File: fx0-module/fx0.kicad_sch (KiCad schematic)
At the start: 15 parts

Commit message: Add pcb draft
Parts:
- added U3: (no value), symbol promicro:ProMicro
- R1: value (none) -> 1K
- R2: value (none) -> 2K
- R3: value (none) -> 5K
- R4: value (none) -> 150K
- R5: value (none) -> 10K
- RF1: renamed from RF; value (none) -> idk
- RI1: renamed from RI; value (none) -> idk
- U2: value (none) -> Pico; footprint (none) -> RPi_Pico:RPi_Pico_SMD_TH
- ULIN1: renamed from ULIN; value (none) -> OPAMP
- renumbered UCVOUT to UCVOUT1
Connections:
- net CVOUT: now also U3.13 (B6)
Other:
- moved on the sheet: R3, R4, R5, UCVOUT1

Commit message: Finish up the fx0 board project
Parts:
- removed RF1, RI1: idk, symbol Device:R
- added C1: 1uF, Capacitor_SMD:C_0805_2012Metric_Pad1.18x1.45mm_HandSolder, symbol Device:C_Small
- added CLINOUT1: 33nF, Capacitor_SMD:C_0805_2012Metric_Pad1.18x1.45mm_HandSolder, symbol Device:C_Small
- added CLINOUT2: 10uF, Capacitor_SMD:C_0805_2012Metric_Pad1.18x1.45mm_HandSolder, symbol Device:C_Small
- added RLIN1, RLIN2, RLIN3: 100, Resistor_SMD:R_0805_2012Metric_Pad1.20x1.40mm_HandSolder, symbol Device:R
- added RLINOUT1, RRLINOUT5: 3.9k, Resistor_SMD:R_0805_2012Metric_Pad1.20x1.40mm_HandSolder, symbol Device:R
- added RLINOUT2: 10K, Resistor_SMD:R_0805_2012Metric_Pad1.20x1.40mm_HandSolder, symbol Device:R
- added RLINOUT3: 5K, Resistor_SMD:R_0805_2012Metric_Pad1.20x1.40mm_HandSolder, symbol Device:R
- added RLINOUT4: 150K, Resistor_SMD:R_0805_2012Metric_Pad1.20x1.40mm_HandSolder, symbol Device:R
- added ULINOUT1: LM358AD, Package_SO:SOP-8_3.9x4.9mm_P1.27mm, symbol pspice:OPAMP
- J1: value (none) -> Line IN; footprint (none) -> Connector_Wire:SolderWirePad_2x01_SMD_1x2mm
- J2: value (none) -> CV IN; footprint (none) -> Connector_Wire:SolderWirePad_2x01_SMD_1x2mm
- J3: value (none) -> Line OUT; footprint (none) -> Connector_Wire:SolderWirePad_2x01_SMD_1x2mm
- J4: value (none) -> CV OUT; footprint (none) -> Connector_Wire:SolderWirePad_2x01_SMD_1x2mm
- RCVIN1: renamed from R2; footprint (none) -> Resistor_SMD:R_0805_2012Metric_Pad1.20x1.40mm_HandSolder
- RCVIN2: renamed from R1; footprint (none) -> Resistor_SMD:R_0805_2012Metric_Pad1.20x1.40mm_HandSolder
- RCVOUT1: renamed from R5; footprint (none) -> Resistor_SMD:R_0805_2012Metric_Pad1.20x1.40mm_HandSolder
- RCVOUT2: renamed from R3; footprint (none) -> Resistor_SMD:R_0805_2012Metric_Pad1.20x1.40mm_HandSolder
- RRCVOUT3: renamed from R4; footprint (none) -> Resistor_SMD:R_0805_2012Metric_Pad1.20x1.40mm_HandSolder
- U1: value (none) -> SeeeduinoXIAO; footprint (none) -> Seeeduino XIAO KICAD:Seeeduino XIAO-MOUDLE14P-2.54-21X17.8MM
- U2: footprint RPi_Pico:RPi_Pico_SMD_TH -> MCU_RaspberryPi_and_Boards:RPi_Pico_SMD_TH
- U3: value (none) -> ProMicro; footprint (none) -> promicro:ProMicro
- UCVOUT1, ULIN1: value OPAMP -> LM358AD; footprint (none) -> Package_SO:SOP-8_3.9x4.9mm_P1.27mm
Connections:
- net 3V3: now also ULIN1.4 (V+), RLIN3.2
- net GND: now also J1.S, J2.S, J3.S, RCVIN1.1, U1.13 (GND), U2.18 (GND), U3.23 (GND), UCVOUT1.5 (V-), ULIN1.5 (V-), CLINOUT1.2, RLIN2.1, RLINOUT2.2, RRLINOUT5.1, ULINOUT1.5 (V-)
- net LINC: now also ULIN1.2 (-)
- net LOUT: now also RLINOUT1.2
- net 5V: now reaches U1.14 (5V)
- net 5V: now also U2.20 (GPIO15), U3.24 (RAW), UCVOUT1.4 (V+), ULINOUT1.4 (V+)
- net at ULIN1.1 (+): now also RLIN1.2, RLIN2.2, RLIN3.1; no longer J1.S
- net at J1.T: now also C1.1
- net LINOUTC: now reaches J3.T
- net LINOUTC: now also CLINOUT2.2, RRLINOUT5.2
- new net: CLINOUT2.1, RLINOUT4.2, ULINOUT1.3
- new net: CLINOUT1.1, RLINOUT1.1, ULINOUT1.1 (+)
- new net: RLINOUT2.1, RLINOUT3.1, ULINOUT1.2 (-)
- new net: C1.2, RLIN1.1
- new net: RLINOUT3.2, RLINOUT4.1
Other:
- note removed: "LINC = RF/RI*LINEIN"
- moved on the sheet: J1, J2, J3, J4, RCVIN1, RCVIN2, RCVOUT1, RCVOUT2, RRCVOUT3, U1, U2, U3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

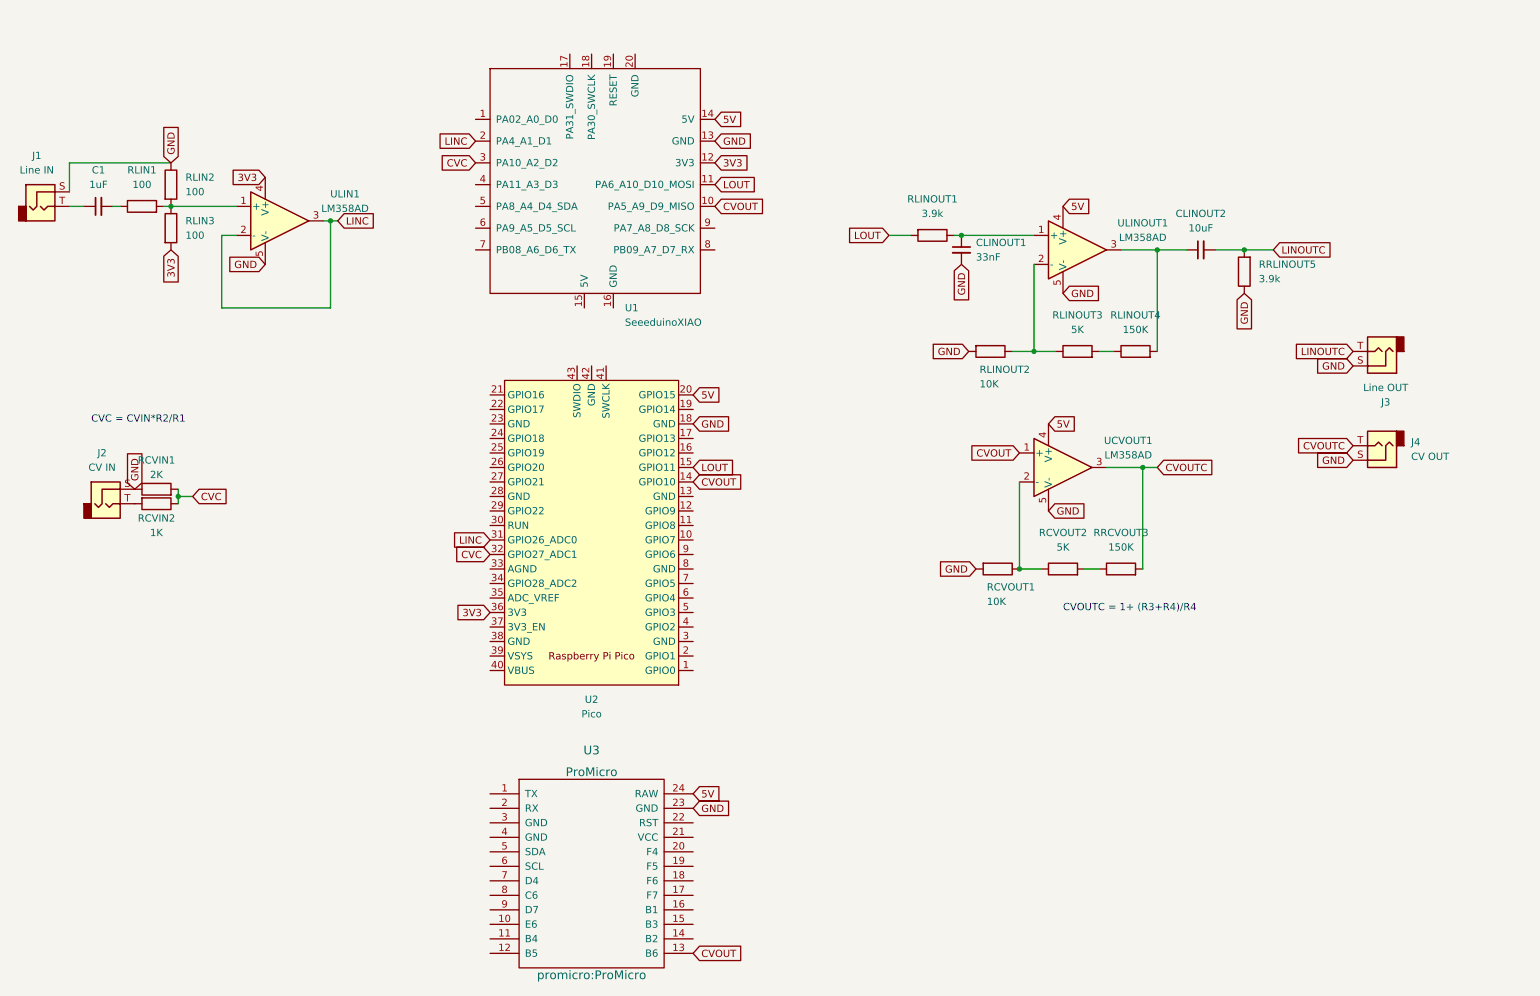
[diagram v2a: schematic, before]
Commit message: Add ground plane and decouple opamps
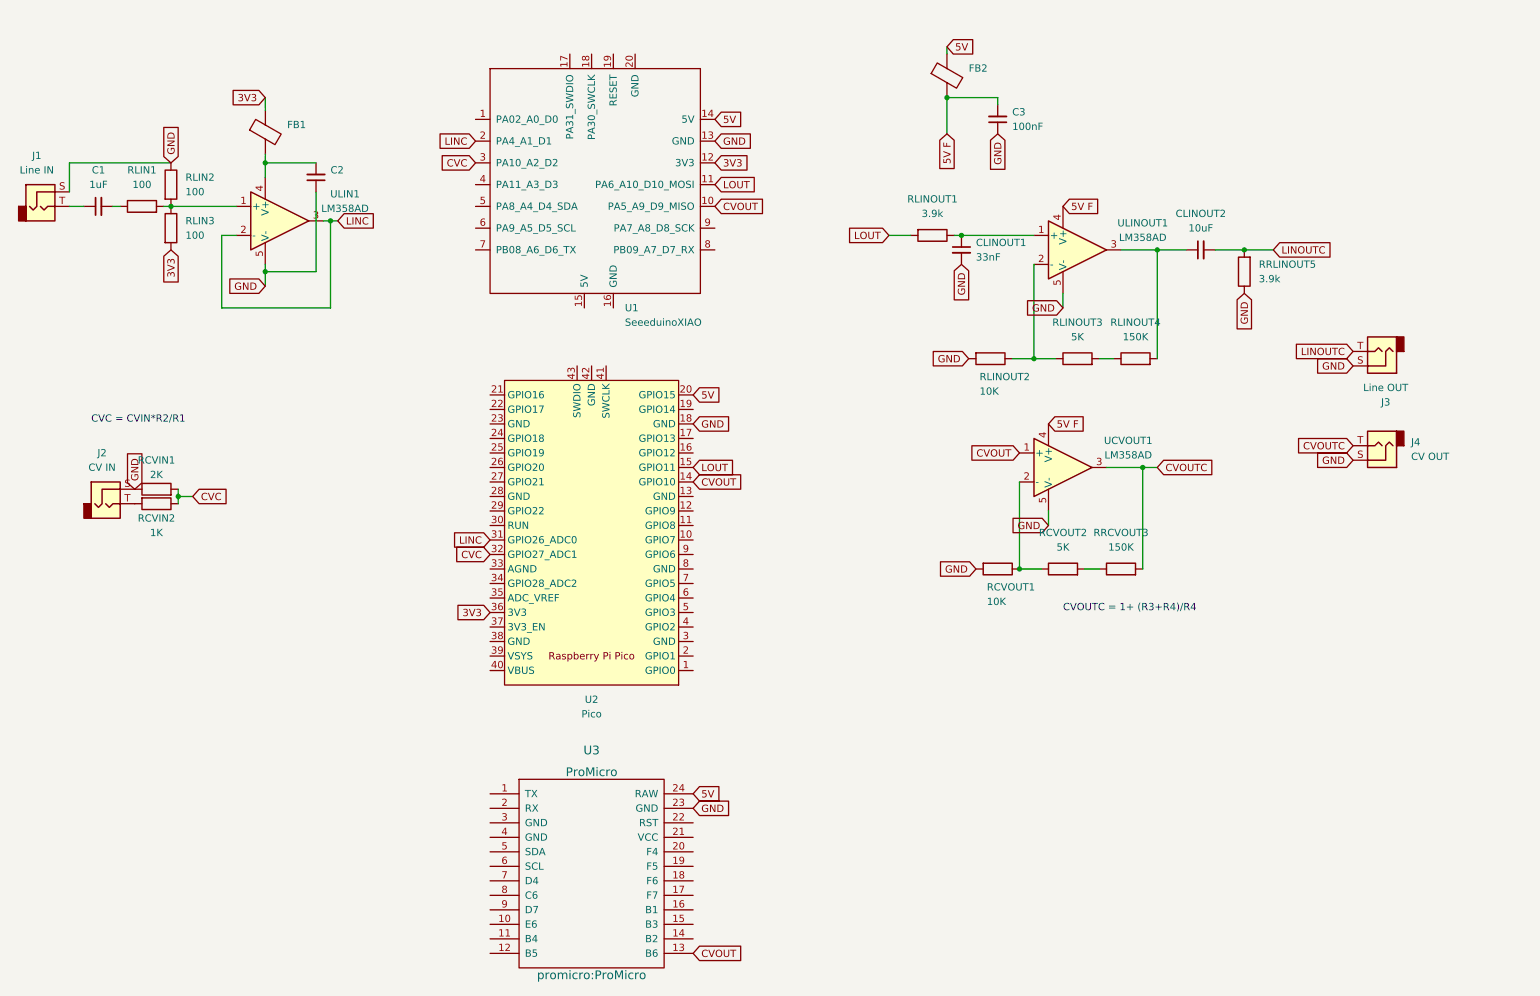
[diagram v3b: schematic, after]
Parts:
- added C2: (no value), Capacitor_SMD:C_0805_2012Metric_Pad1.18x1.45mm_HandSolder, symbol Device:C_Small
- added C3: 100nF, Capacitor_SMD:C_0805_2012Metric_Pad1.18x1.45mm_HandSolder, symbol Device:C_Small
- added FB1, FB2: (no value), symbol Device:FerriteBead
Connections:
- net 3V3: now also FB1.1; no longer ULIN1.4 (V+)
- net 5V: now also FB2.1; no longer UCVOUT1.4 (V+), ULINOUT1.4 (V+)
- net GND: now also C2.1, C3.1
- new net: C2.2, FB1.2, ULIN1.4 (V+)
- new net 5V F: C3.2, FB2.2, UCVOUT1.4 (V+), ULINOUT1.4 (V+)
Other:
- moved on the sheet: RLINOUT2, RLINOUT3, RLINOUT4

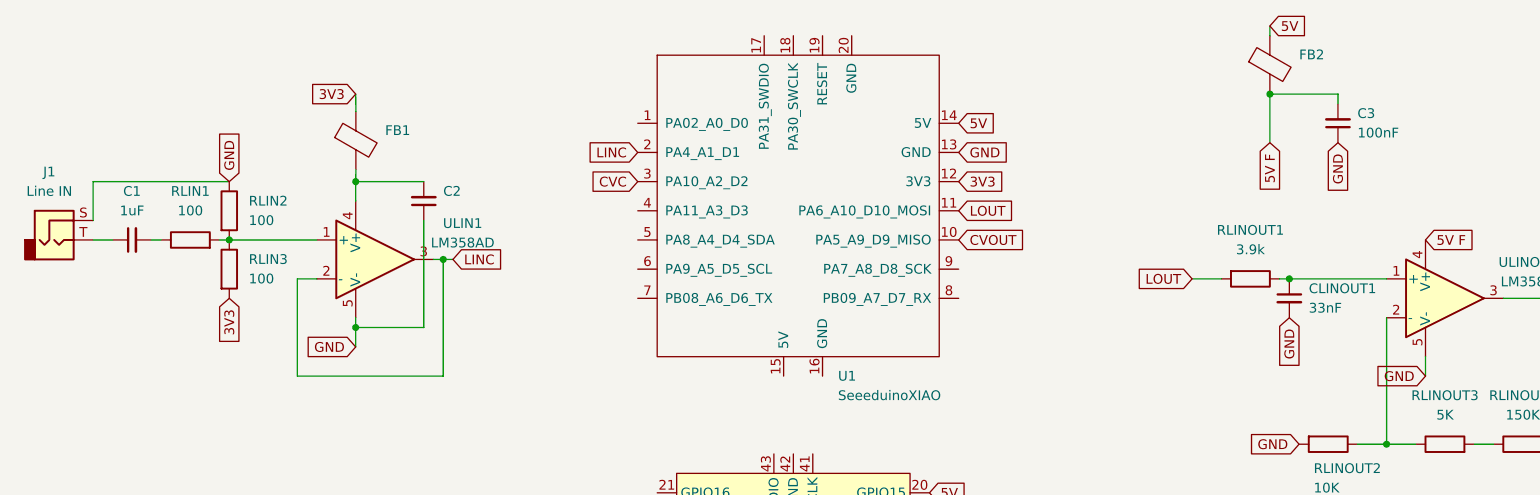
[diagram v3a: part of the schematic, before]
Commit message: Fix buzzing voltage on line in
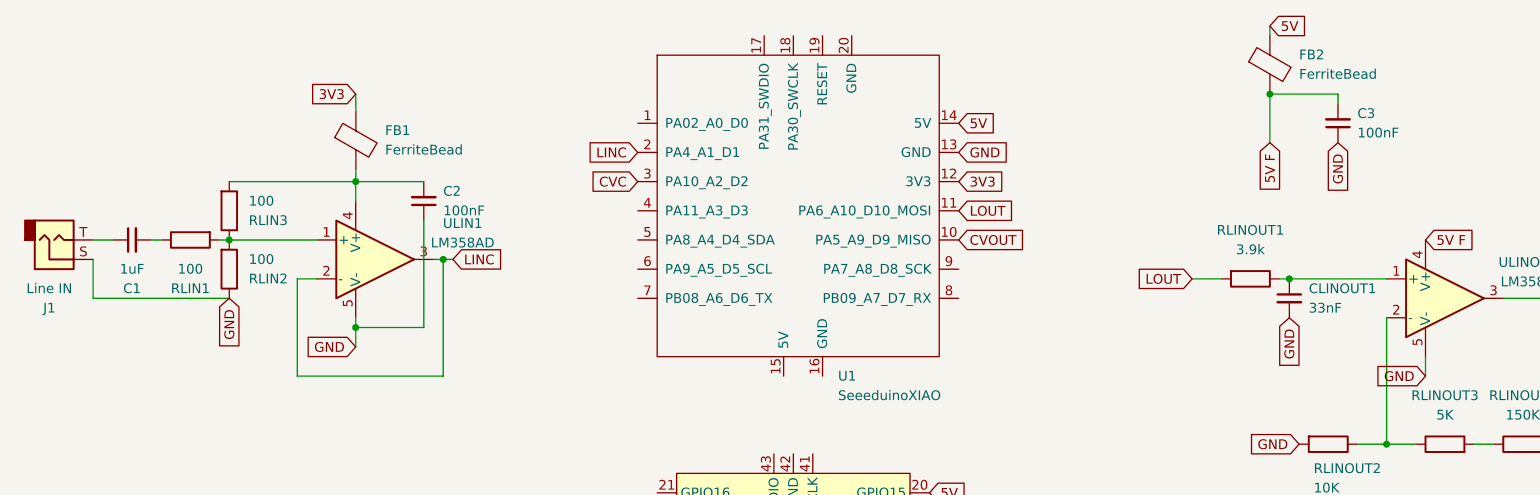
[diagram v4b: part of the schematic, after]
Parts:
- C2: value (none) -> 100nF
- FB1, FB2: value (none) -> FerriteBead; footprint (none) -> Resistor_SMD:R_0805_2012Metric_Pad1.20x1.40mm_HandSolder
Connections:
- net 3V3: no longer RLIN3.2
- net at C2.2, FB1.2, ULIN1.4 (V+): now also RLIN3.2
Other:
- moved on the sheet: J1, RLIN2, RLIN3
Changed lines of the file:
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@@
     (stroke (width 0) (type default) (color 0 0 0 0))
   )
-  (wire (pts (xy 40.64 41.91) (xy 22.86 41.91))
+  (wire (pts (xy 40.64 57.15) (xy 22.86 57.15))
     (stroke (width 0) (type default) (color 0 0 0 0))
   )
@@
     (stroke (width 0) (type default) (color 0 0 0 0))
   )
-  (wire (pts (xy 22.86 41.91) (xy 22.86 46.99))
+  (wire (pts (xy 22.86 57.15) (xy 22.86 52.07))
     (stroke (width 0) (type default) (color 0 0 0 0))
   )
@@
   )
   (wire (pts (xy 49.53 54.61) (xy 49.53 67.31))
+    (stroke (width 0) (type default) (color 0 0 0 0))
+  )
+  (wire (pts (xy 40.64 41.91) (xy 57.15 41.91))
     (stroke (width 0) (type default) (color 0 0 0 0))
   )
@@
     )
   )
-  (global_label "GND" (shape input) (at 40.64 41.91 90) (fields_autoplaced)
-    (effects (font (size 1.27 1.27)) (justify left))
-    (property "Intersheet References" "${INTERSHEET_REFS}" (id 0) (at 40.7194 35.6264 90)
+  (global_label "GND" (shape input) (at 40.64 57.15 270) (fields_autoplaced)
+    (effects (font (size 1.27 1.27)) (justify right))
+    (property "Intersheet References" "${INTERSHEET_REFS}" (id 0) (at 40.7194 63.4336 90)
       (effects (font (size 1.27 1.27)) (justify left) hide)
     )
@@
     (property "Intersheet References" "${INTERSHEET_REFS}" (id 0) (at 243.955 57.0706 0)
       (effects (font (size 1.27 1.27)) (justify left) hide)
-    )
-  )
-  (global_label "3V3" (shape input) (at 40.64 57.15 270) (fields_autoplaced)
-    (effects (font (size 1.27 1.27)) (justify right))
-    (property "Intersheet References" "${INTERSHEET_REFS}" (id 0) (at 40.7194 63.0707 90)
-      (effects (font (size 1.27 1.27)) (justify right) hide)
     )
   )
@@
     (pin "2")
   )
-  (symbol (lib_id "Device:C_Small") (at 27.94 49.53 90) (unit 1)
-    (in_bom yes) (on_board yes) (fields_autoplaced)
-    (property "Reference" "C1" (id 0) (at 27.9463 43.18 90))
-    (property "Value" "1uF" (id 1) (at 27.9463 45.72 90))
+  (symbol (lib_id "Device:C_Small") (at 27.94 49.53 90) (mirror x) (unit 1)
+    (in_bom yes) (on_board yes) (fields_autoplaced)
+    (property "Reference" "C1" (id 0) (at 27.9463 55.88 90))
+    (property "Value" "1uF" (id 1) (at 27.9463 53.34 90))
     (property "Footprint" "Capacitor_SMD:C_0805_2012Metric_Pad1.18x1.45mm_HandSolder" (id 2) (at 27.94 49.53 0)
       (effects (font (size 1.27 1.27)) hide)
@@
       (effects (font (size 1.27 1.27)) (justify left))
     )
-    (property "Value" "" (id 1) (at 180.34 27.8891 0)
-      (effects (font (size 1.27 1.27)) (justify left))
-    )
-    (property "Footprint" "" (id 2) (at 174.752 26.67 90)
+    (property "Value" "FerriteBead" (id 1) (at 180.34 27.8891 0)
+      (effects (font (size 1.27 1.27)) (justify left))
+    )
+    (property "Footprint" "Resistor_SMD:R_0805_2012Metric_Pad1.20x1.40mm_HandSolder" (id 2) (at 174.752 26.67 90)
       (effects (font (size 1.27 1.27)) hide)
     )
@@
     (pin "2")
   )
-  (symbol (lib_id "Device:R") (at 40.64 53.34 0) (unit 1)
+  (symbol (lib_id "Device:R") (at 40.64 45.72 0) (mirror x) (unit 1)
     (in_bom yes) (on_board yes)
-    (property "Reference" "RLIN3" (id 0) (at 43.18 52.0699 0)
-      (effects (font (size 1.27 1.27)) (justify left))
-    )
-    (property "Value" "100" (id 1) (at 43.18 54.6099 0)
+    (property "Reference" "RLIN3" (id 0) (at 43.18 46.9901 0)
+      (effects (font (size 1.27 1.27)) (justify left))
+    )
+    (property "Value" "100" (id 1) (at 43.18 44.4501 0)
+      (effects (font (size 1.27 1.27)) (justify left))
+    )
+    (property "Footprint" "Resistor_SMD:R_0805_2012Metric_Pad1.20x1.40mm_HandSolder" (id 2) (at 38.862 45.72 90)
+      (effects (font (size 1.27 1.27)) hide)
+    )
+    (property "Datasheet" "~" (id 3) (at 40.64 45.72 0)
+      (effects (font (size 1.27 1.27)) hide)
+    )
+    (pin "1")
+    (pin "2")
+  )
+  (symbol (lib_id "Device:R") (at 40.64 53.34 0) (mirror x) (unit 1)
+    (in_bom yes) (on_board yes)
+    (property "Reference" "RLIN2" (id 0) (at 43.18 54.6101 0)
+      (effects (font (size 1.27 1.27)) (justify left))
+    )
+    (property "Value" "100" (id 1) (at 43.18 52.0701 0)
       (effects (font (size 1.27 1.27)) (justify left))
     )
@@
     (pin "2")
   )
-  (symbol (lib_id "Device:R") (at 40.64 45.72 0) (unit 1)
-    (in_bom yes) (on_board yes)
-    (property "Reference" "RLIN2" (id 0) (at 43.18 44.4499 0)
-      (effects (font (size 1.27 1.27)) (justify left))
-    )
-    (property "Value" "100" (id 1) (at 43.18 46.9899 0)
-      (effects (font (size 1.27 1.27)) (justify left))
-    )
-    (property "Footprint" "Resistor_SMD:R_0805_2012Metric_Pad1.20x1.40mm_HandSolder" (id 2) (at 38.862 45.72 90)
-      (effects (font (size 1.27 1.27)) hide)
-    )
-    (property "Datasheet" "~" (id 3) (at 40.64 45.72 0)
-      (effects (font (size 1.27 1.27)) hide)
-    )
-    (pin "1")
-    (pin "2")
-  )
-  (symbol (lib_id "Device:R") (at 35.56 49.53 90) (unit 1)
-    (in_bom yes) (on_board yes) (fields_autoplaced)
-    (property "Reference" "RLIN1" (id 0) (at 35.56 43.18 90))
-    (property "Value" "100" (id 1) (at 35.56 45.72 90))
-    (property "Footprint" "Resistor_SMD:R_0805_2012Metric_Pad1.20x1.40mm_HandSolder" (id 2) (at 35.56 51.308 90)
+  (symbol (lib_id "Device:R") (at 35.56 49.53 90) (mirror x) (unit 1)
+    (in_bom yes) (on_board yes) (fields_autoplaced)
+    (property "Reference" "RLIN1" (id 0) (at 35.56 55.88 90))
+    (property "Value" "100" (id 1) (at 35.56 53.34 90))
+    (property "Footprint" "Resistor_SMD:R_0805_2012Metric_Pad1.20x1.40mm_HandSolder" (id 2) (at 35.56 47.752 90)
       (effects (font (size 1.27 1.27)) hide)
     )
@@
     (pin "2")
   )
-  (symbol (lib_id "Connector:AudioJack2") (at 17.78 49.53 0) (unit 1)
-    (in_bom yes) (on_board yes) (fields_autoplaced)
-    (property "Reference" "J1" (id 0) (at 17.145 40.64 0))
-    (property "Value" "Line IN" (id 1) (at 17.145 43.18 0))
+  (symbol (lib_id "Connector:AudioJack2") (at 17.78 49.53 0) (mirror x) (unit 1)
+    (in_bom yes) (on_board yes) (fields_autoplaced)
+    (property "Reference" "J1" (id 0) (at 17.145 58.42 0))
+    (property "Value" "Line IN" (id 1) (at 17.145 55.88 0))
     (property "Footprint" "Connector_Wire:SolderWirePad_2x01_SMD_1x2mm" (id 2) (at 17.78 49.53 0)
       (effects (font (size 1.27 1.27)) hide)
@@
       (effects (font (size 1.27 1.27)) (justify right))
     )
-    (property "Value" "" (id 1) (at 68.58 45.7135 0)
+    (property "Value" "100nF" (id 1) (at 68.58 45.7135 0)
       (effects (font (size 1.27 1.27)) (justify right))
     )
@@
       (effects (font (size 1.27 1.27)) (justify left))
     )
-    (property "Value" "" (id 1) (at 60.9843 37.7759 0)
-      (effects (font (size 1.27 1.27)) (justify left))
-    )
-    (property "Footprint" "" (id 2) (at 55.3963 36.5568 90)
-      (effects (font (size 1.27 1.27)) hide)
-    )
+    (property "Value" "FerriteBead" (id 1) (at 60.9843 37.7759 0)
+      (effects (font (size 1.27 1.27)) (justify left))
+    )
+    (property "Footprint" "Resistor_SMD:R_0805_2012Metric_Pad1.20x1.40mm_HandSolder" (id 2) (at 55.3963 36.5568 90)
+      (effects (font (size 1.27 1.27)) hide)
+    )
